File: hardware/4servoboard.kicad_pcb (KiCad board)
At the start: 4 copper layers, 23.4 x 30.3 mm, 36 parts, among them J1 USB_C_Receptacle, J2 UART, J3 PWM, J4 V_SERVO, J5 GND, J6 EXT_POWER, J7 DEBUG, Q1 AO3407A, U1 CH32X035F7P6, U2 ME6209A33M3G

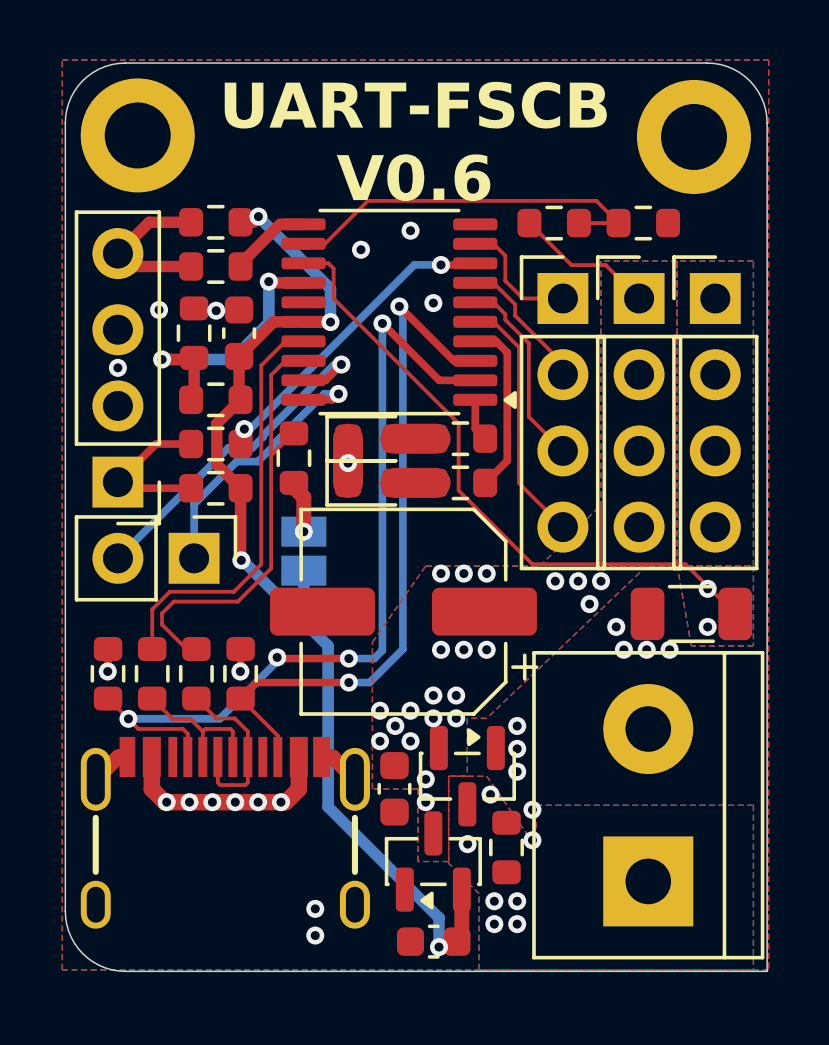
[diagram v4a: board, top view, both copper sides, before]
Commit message: Update: V0.7移行．ORing回路実装，電源設計の効率化，回路定数の見直し
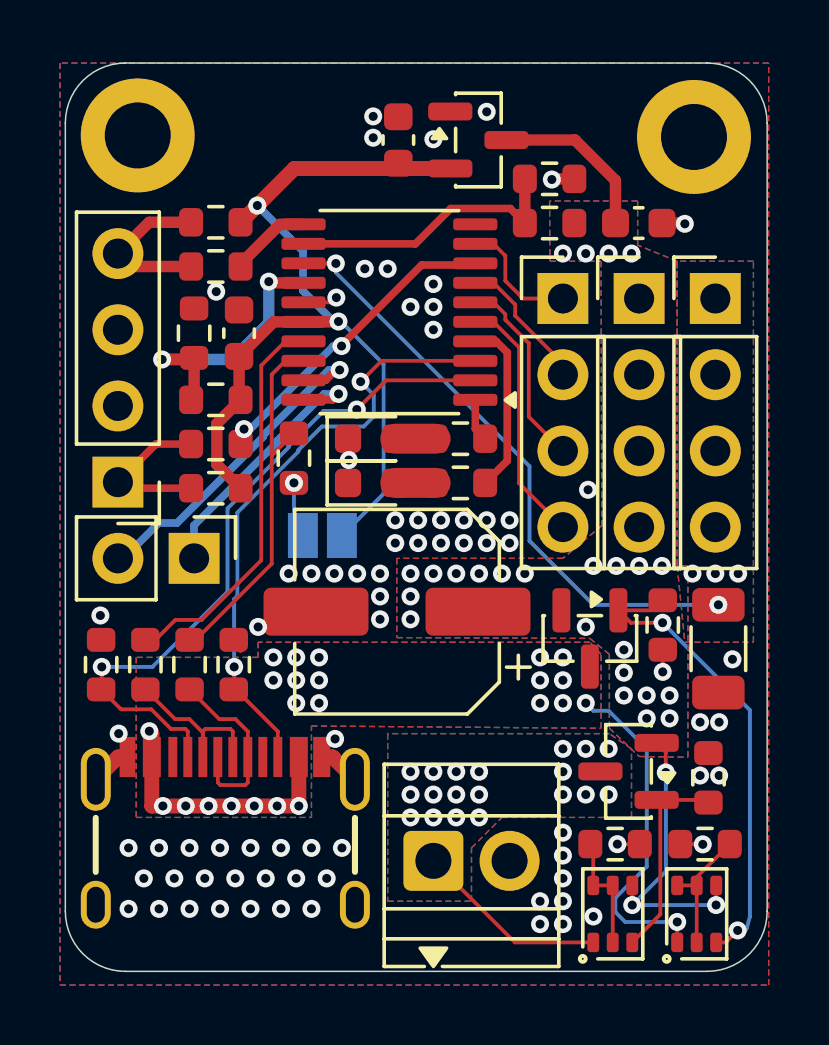
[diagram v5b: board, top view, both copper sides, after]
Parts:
- added Q2: BC857BSs, PCM_Package_TO_SOT_SMD_AKL:SOT-363_SC-70-6, F.Cu at (168.3, 117.0)
- added Q3: BC857BSs, PCM_Package_TO_SOT_SMD_AKL:SOT-363_SC-70-6, F.Cu at (165.5, 117.0)
- added Q4: SI2393DS, Package_TO_SOT_SMD:SOT-23, F.Cu at (166.0, 112.3)
- added R17: 5k1, Resistor_SMD:R_0603_1608Metric, F.Cu at (167.2, 107.4)
- added R18: 5k1, Resistor_SMD:R_0603_1608Metric, F.Cu at (165.6, 114.7)
- added R19: 5k1, Resistor_SMD:R_0603_1608Metric, F.Cu at (168.7, 112.5)
- C1: value 220uF/16V -> 470uF/16V
- J6: footprint TerminalBlock:TerminalBlock_bornier-2_P5.08mm -> TerminalBlock:TerminalBlock_Xinya_XY308-2.54-2P_1x02_P2.54mm_Horizontal
- R16, R7: value 120k -> 5k1
- R8: value 5k1 -> 1k
- moved C3 26.7 mm to (158.3, 91.2), turned to 90 degrees
- moved U2 24.1 mm to (161.0, 91.2), turned to 0 degrees
- moved C2 20.5 mm to (166.4, 94.0), turned to 180 degrees
- moved J6 7.20 mm to (159.5, 115.2), turned to 0 degrees
- moved R16 6.62 mm to (168.6, 114.7), turned to 180 degrees
- moved Q1 6.15 mm to (164.7, 107.8)
- moved R8 3.45 mm to (163.4, 92.5)
- moved R15 1.47 mm to (169.0, 108.2), turned to -90 degrees
- moved JP1 0.81 mm to (155.8, 104.4), turned to 0 degrees
- moved R1 0.38 mm to (151.4, 108.7)
- moved R2 0.38 mm to (149.9, 108.7)
- moved R3 0.38 mm to (148.4, 108.7)
- moved R4 0.38 mm to (152.9, 108.7)
- moved C1 0.21 mm to (158.3, 106.9)
- moved R7 0.15 mm to (163.4, 94.0), turned to 180 degrees
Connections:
- J6 pad 1: VBUS -> EXT_VIN
- Q1 pad 1: GND -> Net-(Q1-G)
- R16 pad 1: VBUS -> Net-(Q2A-B1)
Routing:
- net Net-(Q1-G): track 0.00 -> 15.9 mm, vias 0 -> 2
- net VBUS: track 7.40 -> 20.7 mm, vias 12 -> 24
- net V_SERVO: track 4.70 -> 15.7 mm, vias 21 -> 27
- net Net-(Q3B-C2): track 0.00 -> 6.95 mm
- net EXT_VIN: track 0.00 -> 6.46 mm, vias 0 -> 19
- net VDD: track 36.1 -> 30.0 mm, vias 4 -> 2
- net CC1: track 28.2 -> 23.1 mm, vias 4 -> 2
- net Net-(Q2A-B1): track 0.00 -> 4.38 mm
- net Net-(Q3A-B1): track 0.00 -> 3.97 mm
- net V_SENSE: track 12.7 -> 9.54 mm
- net CC2: track 23.3 -> 20.2 mm
- net D+: track 14.9 -> 12.4 mm
- net GND: track 6.12 -> 8.10 mm, vias 20 -> 77
- net Net-(J1-D--PadA7): track 4.91 -> 6.10 mm
- net CURRENT_SENSE: track 21.1 -> 20.2 mm, vias 2 -> 5
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- added copper zone on B.Cu, net EXT_VIN
- added copper zone on F.Cu, net EXT_VIN
- added copper zone on In1.Cu, net EXT_VIN
- added copper zone on In2.Cu, net EXT_VIN
- removed copper zone on In1.Cu, net VBUS
- removed copper zone on In2.Cu, net VBUS
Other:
- outline, holes or cut-outs redrawn
- board text added: "R3"
- board text added: "UART-FSCB V0.7"
- board text removed: "+"
- board text removed: "UART-FSCB V0.6"

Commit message: Update: V0.8移行．回路設計の効率化．エラッタの修正
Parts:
- JP1: moved to F.Cu
- moved JP1 13.9 mm to (155.7, 90.5)
- moved R9 10.5 mm to (153.3, 91.5), turned to -90 degrees
- moved D1 2.96 mm to (160.4, 102.6)
- moved R5 2.96 mm to (157.5, 102.6)
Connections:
- D1 pad 1: GND -> Net-(D1-K)
- D1 pad 2: Net-(D1-A) -> MCU_LED2
- R5 pad 1: Net-(D1-A) -> VDD
- R5 pad 2: MCU_LED2 -> Net-(D1-K)
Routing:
- net D+: track 12.4 -> 24.1 mm, vias 0 -> 2
- net Net-(D1-A): track 1.35 -> 0.00 mm
- net Net-(D1-K): track 0.00 -> 1.35 mm
- net CURRENT_SENSE: track 20.2 -> 19.3 mm
- net Net-(Q1-G): track 15.9 -> 16.6 mm
- net GND: track 8.10 -> 8.65 mm
- net VDD: track 30.0 -> 30.5 mm, vias 2 -> 3
- net Net-(JP1-A): track 1.88 -> 1.81 mm, vias 1 -> 0
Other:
- board text added: "+"
- board text added: "-"
- board text added: "DIO DCK"
- board text added: "UART-FSCB V0.8"
- board text removed: "UART-FSCB V0.7"
